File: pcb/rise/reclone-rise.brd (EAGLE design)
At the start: 85 x 56 mm, 130 parts, among them Y1 12MHz, Y4 32K768

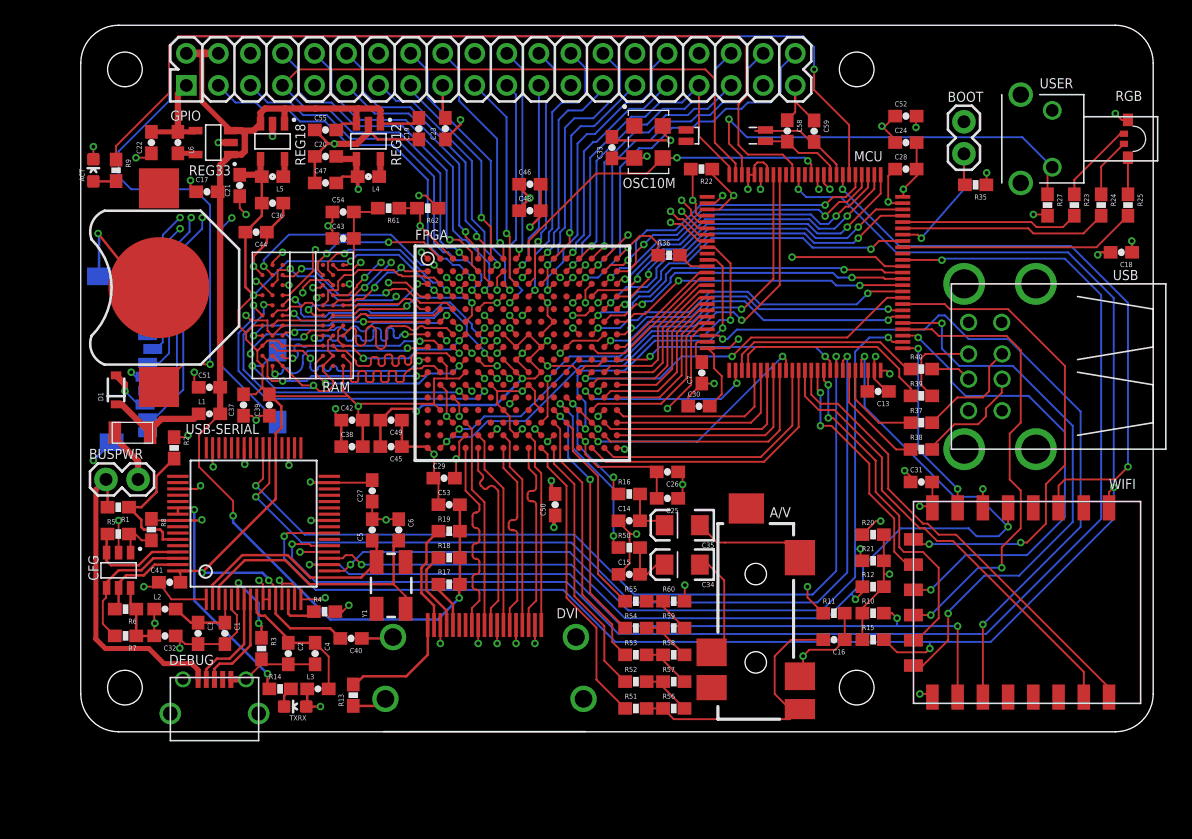
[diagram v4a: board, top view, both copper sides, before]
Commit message: Found alternate pins for video that were previously assigned to M0 and M1; tweaked headphone filter values to take advantage of close to 24mA max per pin
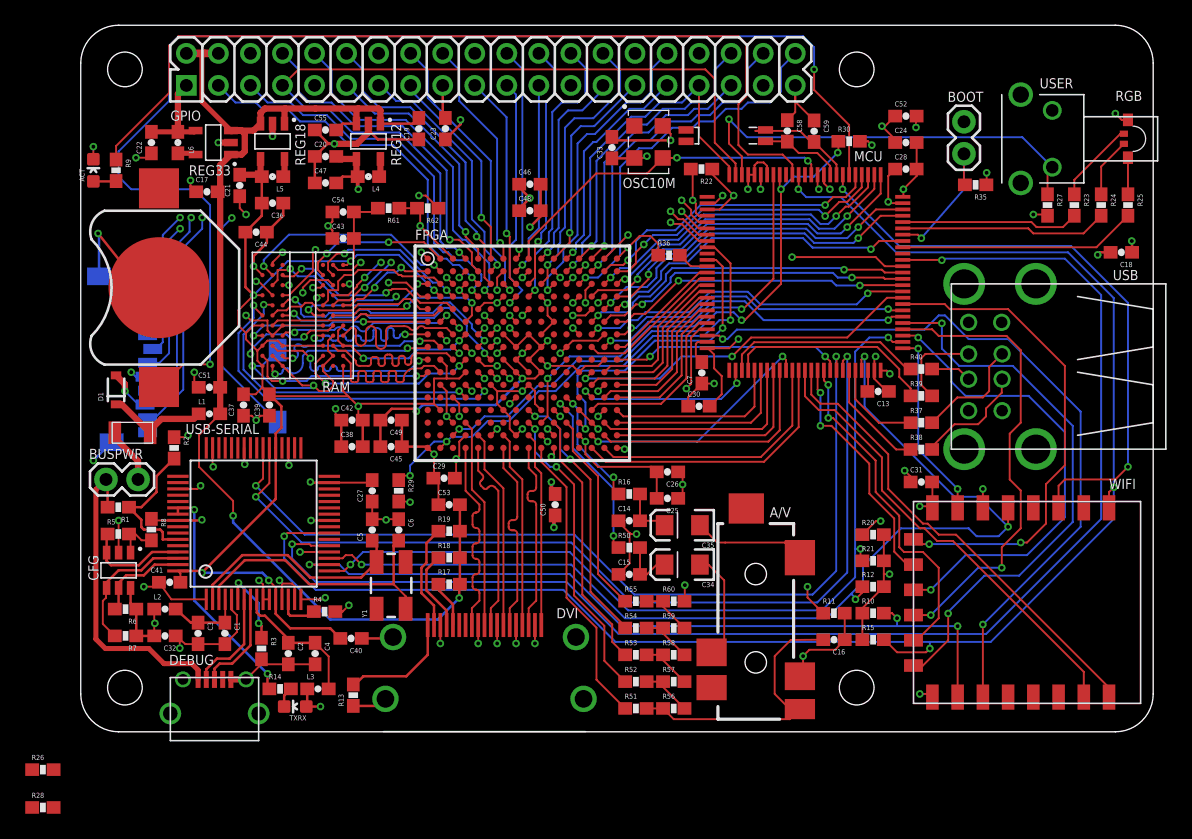
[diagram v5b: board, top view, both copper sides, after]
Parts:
- added R26, R28, R29, R30: 4K7, SparkFun-Passives:0603-RES
- C14, C15: value 47n -> 56n
- R16, R50: value 180 -> 150
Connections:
- removed net M3RESET: FPGA.E4
- removed net WIFI_INT: MCU.91
- new net WIFI_INT_WAKE: MCU.91, WIFI.4
- net +3V3: now also FPGA.N11, FPGA.T11, R29.2, R30.2
- net FPGA_CONFIG_INIT_B: now also R30.1
- net FPGA_CONFIG_PROGRAM_B: now also R29.1
- net GND: now also R26.1, R28.1
- net M3CKE: now also R28.2
- net M3ODT: now also R26.2
- net VIDEO_D1: now also FPGA.N9; no longer FPGA.N11
- net VIDEO_D3: now also FPGA.P9; no longer FPGA.T11
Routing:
- net FPGA_CONFIG_INIT_B: track 40.1 -> 46.8 mm, vias 2 -> 4
- net FPGA_CONFIG_PROGRAM_B: track 34.1 -> 39.6 mm, vias 2 -> 3
- net +3V3: track 123.6 -> 127.1 mm, vias 34 -> 38
- net VIDEO_D3: track 20.9 -> 24.0 mm, vias 0 -> 2
- net FPGA_CONFIG_CLK: track 19.2 -> 21.2 mm
- net VIDEO_D1: track 19.6 -> 21.0 mm
- net JTAG_FPGA_TDO: track 51.9 -> 51.4 mm

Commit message: Routed WIFI_INT, the missing GPIO pin, and a pull-down on the ODT signal
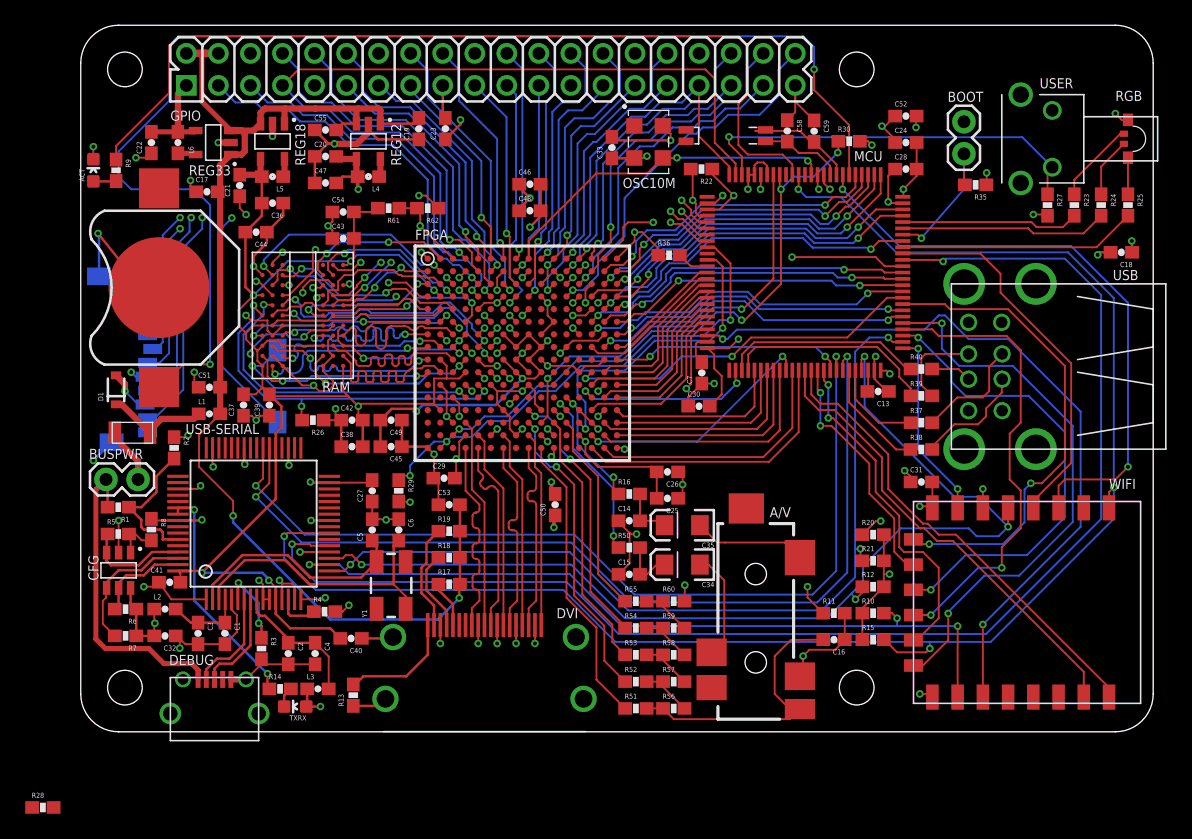
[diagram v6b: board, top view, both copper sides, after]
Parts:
- R36: value 47K -> 10K
- moved R26 35.0 mm to (18.4, 24.7), turned to 180 degrees
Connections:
- net WIFI_INT_WAKE renamed WIFI_INT
- net GPIO25: now also FPGA.C13; no longer FPGA.D12
- net GPIO29: now also FPGA.D12; no longer FPGA.C13
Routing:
- net WIFI_INT: track 0.00 -> 30.5 mm
- net GPIO25: track 0.00 -> 24.7 mm, vias 0 -> 1
- net WKUP: track 34.3 -> 32.3 mm
- net GND: track 234.6 -> 236.5 mm
- net M3ODT: track 28.2 -> 29.9 mm, vias 2 -> 3
- net JTAG_TMS: track 121.4 -> 122.9 mm
- net SDIO_CMD: track 39.3 -> 38.8 mm

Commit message: Placed and routed pull-down resistor for CKE
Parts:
- moved R28 49.6 mm to (17.7, 39.1)
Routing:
- net M3CKE: track 13.5 -> 28.1 mm, vias 2 -> 3
- net FSMC_D1: track 22.7 -> 20.3 mm
- net GND: track 236.5 -> 238.8 mm
- net FSMC_D0: track 20.7 -> 18.4 mm
- net FSMC_A17: track 19.2 -> 17.1 mm
- net FSMC_A16: track 17.1 -> 15.2 mm
- net FSMC_D15: track 17.3 -> 15.6 mm
- net M3A0: track 26.9 -> 25.5 mm
- net FSMC_D14: track 15.1 -> 13.7 mm
- net +1V8: track 134.8 -> 136.1 mm
- net FSMC_D13: track 14.3 -> 13.1 mm
- net M3A7: track 13.0 -> 13.7 mm

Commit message: Added values for two inductors and three ferrite beads
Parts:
- L1, L2, L3: value (none) -> BEAD
- L4, L5: value (none) -> 2u2
- L6: value (none) -> 4u7
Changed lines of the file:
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@@
 <element name="R9" library="SparkFun-Passives" package="0603-RES" value="220" x="2.8" y="44.5" rot="R270"/>
 <element name="F1" library="reclone-rise" package="1206L" value="POLYFUSE" x="4.1" y="23.7"/>
-<element name="L1" library="SparkFun-Passives" package="0603" value="" x="10.2" y="25.2"/>
-<element name="L2" library="SparkFun-Passives" package="0603" value="" x="6.675" y="9.725"/>
-<element name="L3" library="SparkFun-Passives" package="0603" value="" x="18.8" y="3.4"/>
+<element name="L1" library="SparkFun-Passives" package="0603" value="BEAD" x="10.2" y="25.2"/>
+<element name="L2" library="SparkFun-Passives" package="0603" value="BEAD" x="6.675" y="9.725"/>
+<element name="L3" library="SparkFun-Passives" package="0603" value="BEAD" x="18.8" y="3.4"/>
 <element name="D1" library="SparkFun-DiscreteSemi" package="SOD-323" value="5.6V" x="2.8" y="27.1" rot="R90">
 <attribute name="PROD_ID" value="DIO-12442" x="2.8" y="27.1" size="1.778" layer="27" rot="R90" display="off"/>
@@
 <element name="REG18" library="reclone-rise" package="SOT-23-5" value="PAM2305AAB180" x="15.2" y="46.8" rot="R180"/>
 <element name="REG33" library="reclone-rise" package="SOT-23-5" value="PAM2305AAB330" x="10.5" y="46.7" rot="R90"/>
-<element name="L4" library="SparkFun-Passives" package="0603" value="" x="22.8" y="44" rot="R180"/>
-<element name="L5" library="SparkFun-Passives" package="0603" value="" x="15.2" y="44" rot="R180"/>
-<element name="L6" library="SparkFun-Passives" package="0603" value="" x="7.7" y="46.7" smashed="yes" rot="R90">
+<element name="L4" library="SparkFun-Passives" package="0603" value="2u2" x="22.8" y="44" rot="R180"/>
+<element name="L5" library="SparkFun-Passives" package="0603" value="2u2" x="15.2" y="44" rot="R180"/>
+<element name="L6" library="SparkFun-Passives" package="0603" value="4u7" x="7.7" y="46.7" smashed="yes" rot="R90">
 <attribute name="NAME" x="8.938" y="45.811" size="0.4064" layer="25" font="vector" rot="R90"/>
 <attribute name="VALUE" x="8.843" y="45.684" size="0.4064" layer="27" font="vector" rot="R90"/>
